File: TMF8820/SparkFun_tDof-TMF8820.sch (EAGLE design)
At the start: 21 parts, among them J4 QWIIC_RIGHT_ANGLE, J5 QWIIC_RIGHT_ANGLE

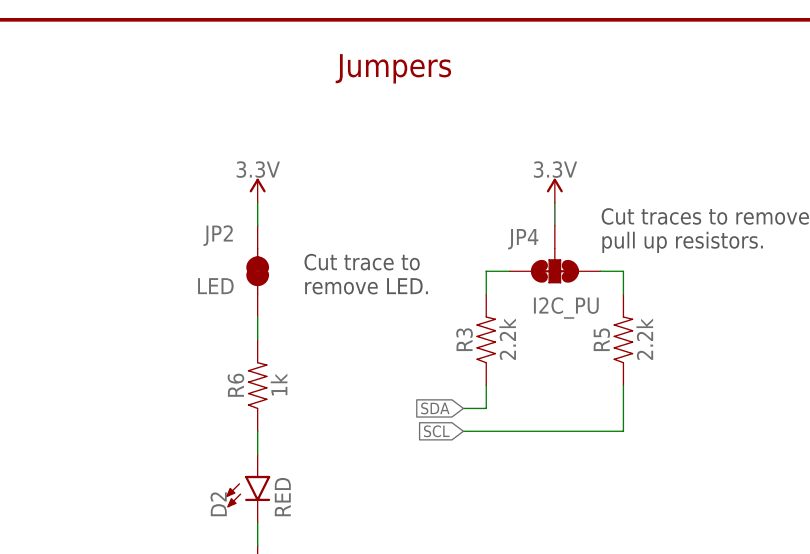
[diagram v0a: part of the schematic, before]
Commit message: Adds an additional folder for second part
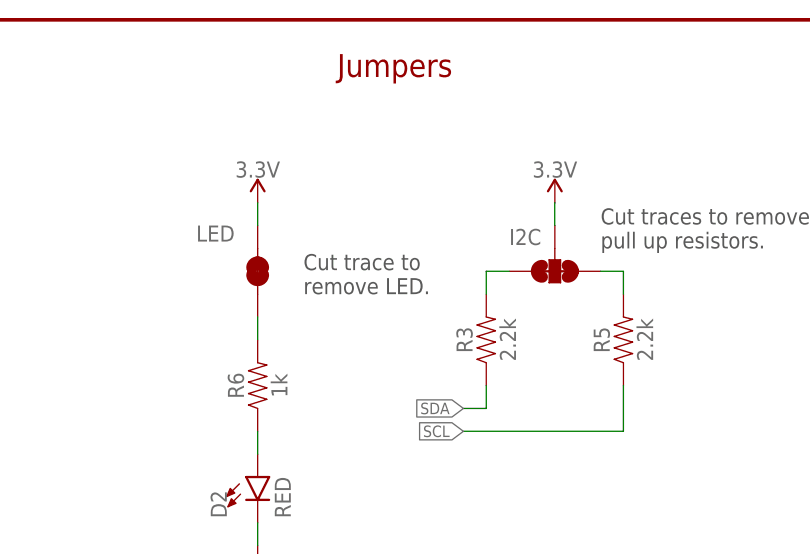
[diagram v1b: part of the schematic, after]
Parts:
- renumbered JP2 to LED, JP4 to I2C
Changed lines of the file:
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@@
 <part name="R6" library="SparkFun-Resistors" deviceset="1KOHM" device="-0603-1/10W-1%" value="1k"/>
 <part name="D2" library="SparkFun-LED" deviceset="LED-RED" device="0603" value="RED"/>
-<part name="JP2" library="SparkFun-Jumpers" deviceset="JUMPER-SMT_2_NC_TRACE" device="_SILK" package3d_urn="urn:adsk.eagle:package:39281/1" value="LED"/>
+<part name="LED" library="SparkFun-Jumpers" deviceset="JUMPER-SMT_2_NC_TRACE" device="_SILK" package3d_urn="urn:adsk.eagle:package:39281/1" value="LED"/>
 <part name="GND8" library="SparkFun-PowerSymbols" deviceset="GND" device=""/>
 <part name="SUPPLY9" library="SparkFun-PowerSymbols" deviceset="3.3V" device=""/>
-<part name="JP4" library="SparkFun-Jumpers" deviceset="JUMPER-SMT_3_2-NC_TRACE" device="_SILK" package3d_urn="urn:adsk.eagle:package:39289/1" value="I2C_PU"/>
+<part name="I2C" library="SparkFun-Jumpers" deviceset="JUMPER-SMT_3_2-NC_TRACE" device="_SILK" package3d_urn="urn:adsk.eagle:package:39289/1" value="I2C_PU"/>
 <part name="SUPPLY10" library="SparkFun-PowerSymbols" deviceset="3.3V" device=""/>
 </parts>
@@
 <attribute name="VALUE" x="182.245" y="130.048" size="1.778" layer="96" font="vector" rot="R90" align="top-left"/>
 </instance>
-<instance part="JP2" gate="G$1" x="180.34" y="157.48" smashed="yes" rot="R90">
+<instance part="LED" gate="G$1" x="180.34" y="157.48" smashed="yes" rot="R90">
 <attribute name="NAME" x="177.8" y="162.56" size="1.778" layer="95" font="vector" rot="R180"/>
-<attribute name="VALUE" x="177.8" y="154.94" size="1.778" layer="96" font="vector" rot="R180" align="top-left"/>
 </instance>
 <instance part="GND8" gate="1" x="180.34" y="124.46" smashed="yes">
@@
 <attribute name="VALUE" x="180.34" y="167.894" size="1.778" layer="96" font="vector" align="bottom-center"/>
 </instance>
-<instance part="JP4" gate="G$1" x="213.36" y="157.48" smashed="yes" rot="R270">
+<instance part="I2C" gate="G$1" x="213.36" y="157.48" smashed="yes" rot="R270">
 <attribute name="NAME" x="208.28" y="160.401" size="1.778" layer="95" font="vector"/>
-<attribute name="VALUE" x="210.82" y="154.559" size="1.778" layer="96" font="vector" align="top-left"/>
 </instance>
 <instance part="SUPPLY10" gate="G$1" x="213.36" y="165.1" smashed="yes">
@@
 </segment>
 <segment>
-<pinref part="JP2" gate="G$1" pin="2"/>
+<pinref part="LED" gate="G$1" pin="2"/>
 <wire x1="180.34" y1="162.56" x2="180.34" y2="165.1" width="0.1524" layer="91"/>
 <pinref part="SUPPLY9" gate="G$1" pin="3.3V"/>
@@
 <segment>
 <pinref part="SUPPLY10" gate="G$1" pin="3.3V"/>
-<pinref part="JP4" gate="G$1" pin="2"/>
+<pinref part="I2C" gate="G$1" pin="2"/>
 <wire x1="213.36" y1="165.1" x2="213.36" y2="162.56" width="0.1524" layer="91"/>
 </segment>
@@
 <segment>
 <pinref part="R6" gate="G$1" pin="2"/>
-<pinref part="JP2" gate="G$1" pin="1"/>
+<pinref part="LED" gate="G$1" pin="1"/>
 <wire x1="180.34" y1="149.86" x2="180.34" y2="152.4" width="0.1524" layer="91"/>
 </segment>
@@
 <pinref part="R3" gate="G$1" pin="2"/>
 <wire x1="205.74" y1="154.94" x2="205.74" y2="157.48" width="0.1524" layer="91"/>
-<pinref part="JP4" gate="G$1" pin="3"/>
+<pinref part="I2C" gate="G$1" pin="3"/>
 <wire x1="205.74" y1="157.48" x2="208.28" y2="157.48" width="0.1524" layer="91"/>
 </segment>
@@
 <net name="N$8" class="0">
 <segment>
-<pinref part="JP4" gate="G$1" pin="1"/>
+<pinref part="I2C" gate="G$1" pin="1"/>
 <wire x1="218.44" y1="157.48" x2="220.98" y2="157.48" width="0.1524" layer="91"/>
 <pinref part="R5" gate="G$1" pin="2"/>

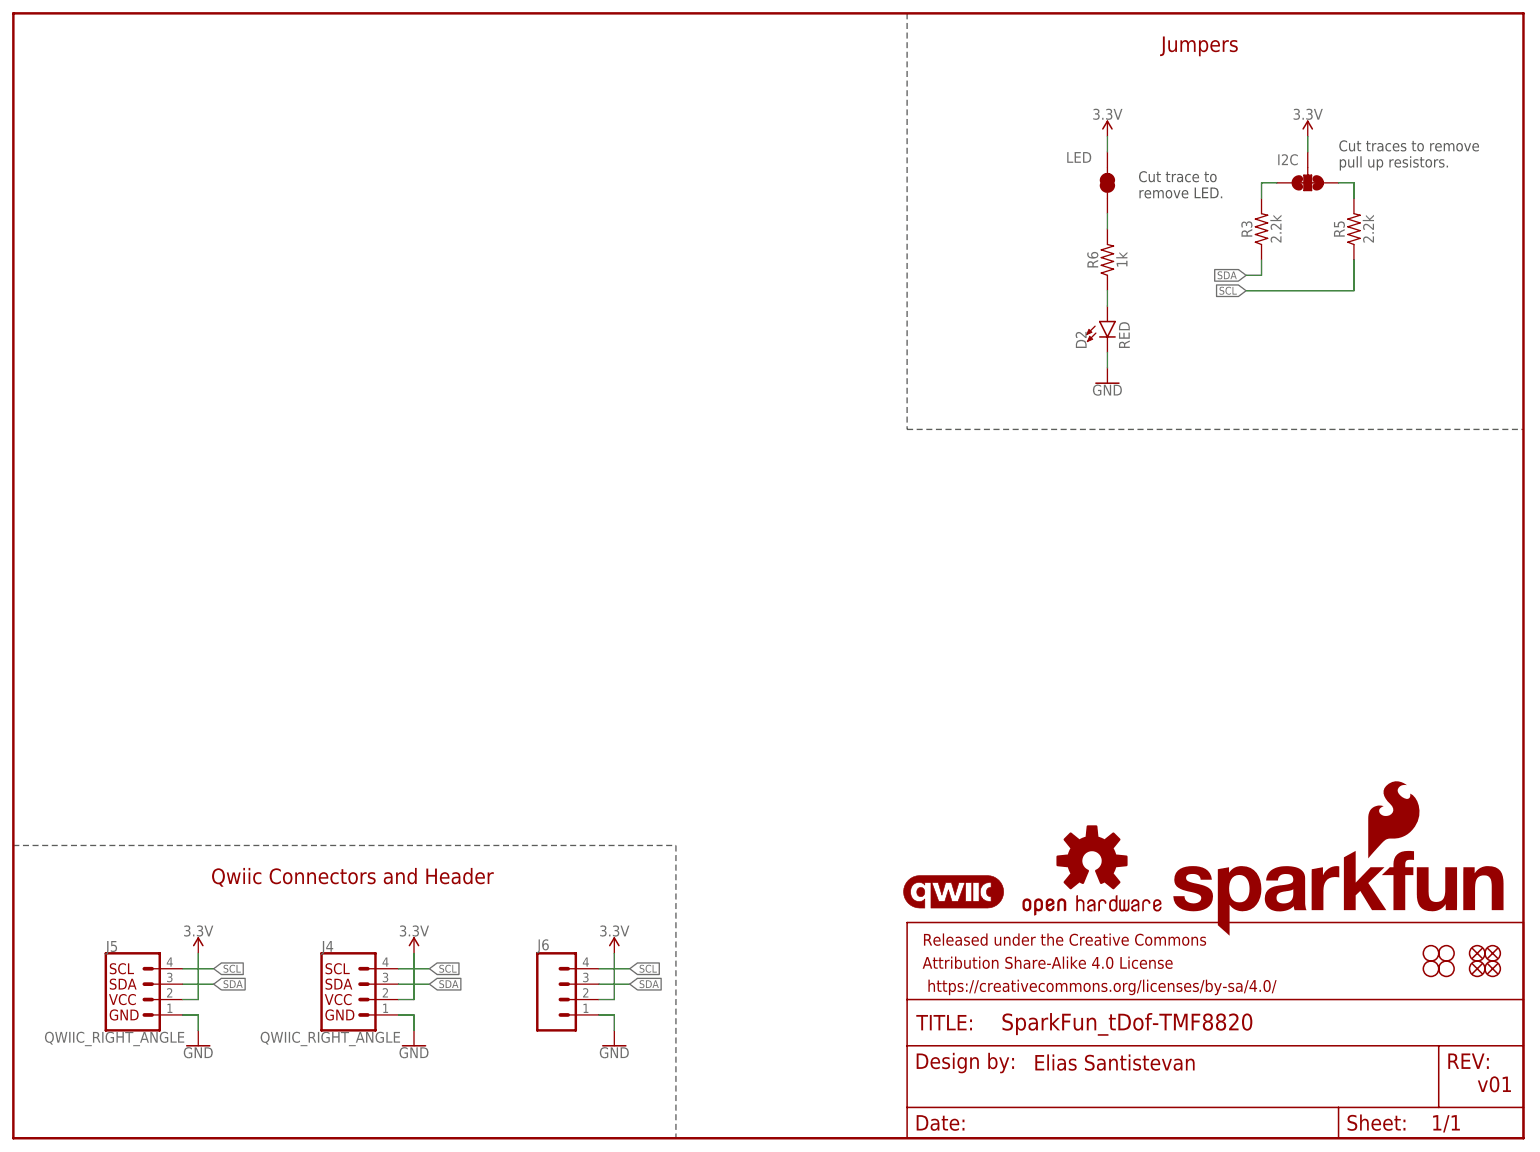
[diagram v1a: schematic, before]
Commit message: Moves correct TMF8820 files into the correct folder
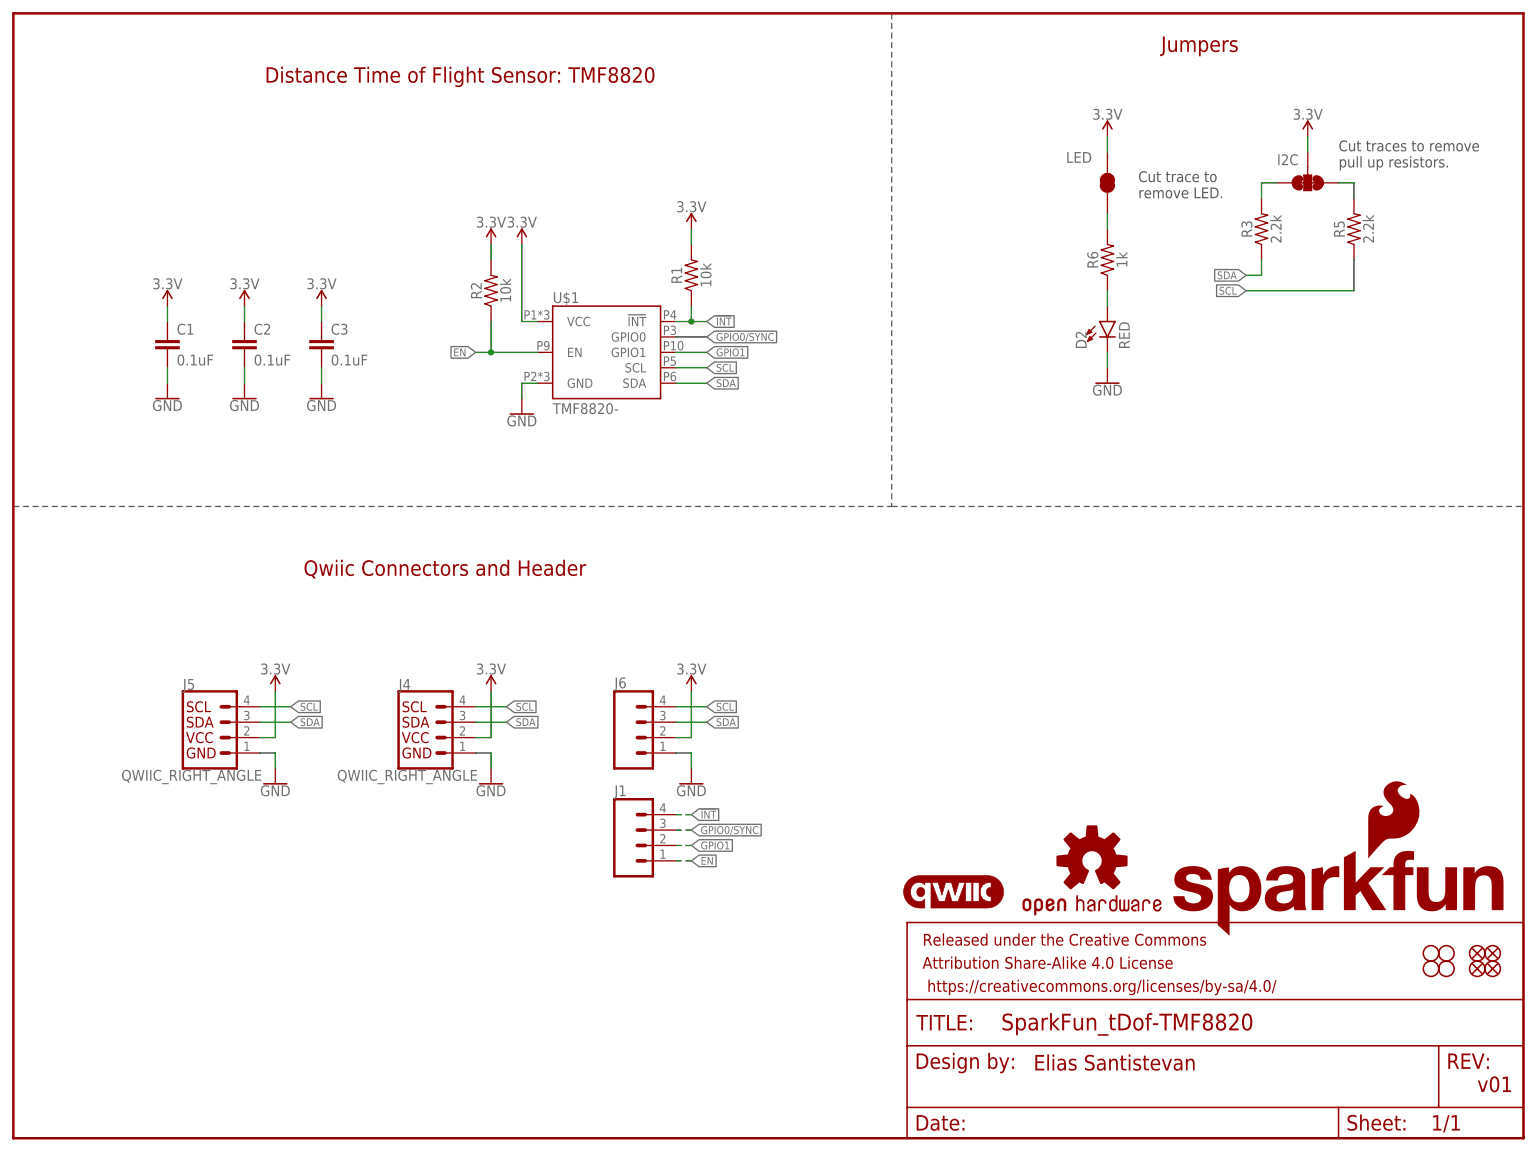
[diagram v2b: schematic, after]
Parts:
- added C1, C2, C3: 0.1uF, SparkFun-Capacitors:0.1UF-0402T-6.3V-10%-X7R
- added J1: (no value), SparkFun-Connectors:CONN_041X04_NO_SILK_NO_POP
- added R1, R2: 10k, SparkFun-Resistors:10KOHM-0603-1/10W-1%
- added U$1: TMF8820-, TMF882X:TMF8820-
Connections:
- new net !INT!: J1.4, R1.1, U$1.!INT!
- new net EN: J1.1, R2.1, U$1.EN
- new net GPIO0/SYNC: J1.3, U$1.GPIO0
- new net GPIO1: J1.2, U$1.GPIO1
- net 3.3V: now also C1.1, C2.1, C3.1, R1.2, R2.2, U$1.VCC
- net GND: now also C1.2, C2.2, C3.2, U$1.GND
- net SCL: now also U$1.SCL
- net SDA: now also U$1.SDA
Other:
- note added: "Distance Time of Flight Sensor: TMF8820"
- moved on the sheet: J4, J5, J6

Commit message: Adds VCC Range to schematic in both designs
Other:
- note added: "VCC Range: 2.7V - 3.3V I/O VCC Range: 1.62V - 3.3V"
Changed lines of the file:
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@@
 <wire x1="144.78" y1="104.14" x2="248.92" y2="104.14" width="0.2032" layer="97" style="longdash"/>
 <wire x1="144.78" y1="185.42" x2="144.78" y2="104.14" width="0.2032" layer="97" style="longdash"/>
+<text x="58.42" y="165.1" size="1.778" layer="97" font="vector">VCC Range: 2.7V - 3.3V
+I/O VCC Range: 1.62V - 3.3V</text>
 </plain>
 <instances>

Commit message: Moves header to one side on the 1"x1" Qwiic Board
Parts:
- removed H7: STAND-OFFTIGHT, SparkFun-Hardware:STAND-OFFTIGHT
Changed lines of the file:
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@@
 <part name="H5" library="SparkFun-Hardware" deviceset="STAND-OFF" device="TIGHT"/>
 <part name="H6" library="SparkFun-Hardware" deviceset="STAND-OFF" device="TIGHT"/>
-<part name="H7" library="SparkFun-Hardware" deviceset="STAND-OFF" device="TIGHT"/>
 <part name="H8" library="SparkFun-Hardware" deviceset="STAND-OFF" device="TIGHT"/>
 <part name="J4" library="SparkFun-Connectors" deviceset="QWIIC_CONNECTOR" device="JS-1MM" value="QWIIC_RIGHT_ANGLE"/>
@@
 <instance part="H5" gate="G$1" x="233.68" y="27.94" smashed="yes"/>
 <instance part="H6" gate="G$1" x="233.68" y="30.48" smashed="yes"/>
-<instance part="H7" gate="G$1" x="236.22" y="30.48" smashed="yes"/>
 <instance part="H8" gate="G$1" x="236.22" y="27.94" smashed="yes"/>
 <instance part="J4" gate="G$1" x="68.58" y="66.04" smashed="yes">

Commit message: Updates the TMF882X device in the library to have two variants of the two ICs
* Better silk labeling for the 8820 and 8820 HQ
* Adds new IC variants to both designs
* Adds default addresses to schematics
* Moves some traces and vias for better ground pour in the 8820 design
* Moves entire 8820 design to origin in board file
* Adds measure from center of qwiic connector to edge in 8820 design
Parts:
- U$1: value TMF8820- -> TMF882X_TMF8820; device TMF882X:TMF8820- -> TMF882X:TMF882X_TMF8820
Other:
- note added: "Default Address: 0x41"
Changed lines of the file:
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@@
 <part name="I2C" library="SparkFun-Jumpers" deviceset="JUMPER-SMT_3_2-NC_TRACE" device="_SILK" package3d_urn="urn:adsk.eagle:package:39289/1" value="I2C_PU"/>
 <part name="SUPPLY10" library="SparkFun-PowerSymbols" deviceset="3.3V" device=""/>
-<part name="U$1" library="TMF882X" deviceset="TMF8820" device="-"/>
+<part name="U$1" library="TMF882X" deviceset="TMF882X" device="_TMF8820"/>
 <part name="C1" library="SparkFun-Capacitors" deviceset="0.1UF" device="-0402T-6.3V-10%-X7R" value="0.1uF"/>
 <part name="C2" library="SparkFun-Capacitors" deviceset="0.1UF" device="-0402T-6.3V-10%-X7R" value="0.1uF"/>
@@
 <text x="58.42" y="165.1" size="1.778" layer="97" font="vector">VCC Range: 2.7V - 3.3V
 I/O VCC Range: 1.62V - 3.3V</text>
+<text x="58.42" y="157.48" size="1.778" layer="97" font="vector">Default Address: 0x41</text>
 </plain>
 <instances>
